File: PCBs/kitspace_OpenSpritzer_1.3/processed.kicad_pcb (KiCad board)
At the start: 2 copper layers, 57.5 x 85 mm, 30 parts

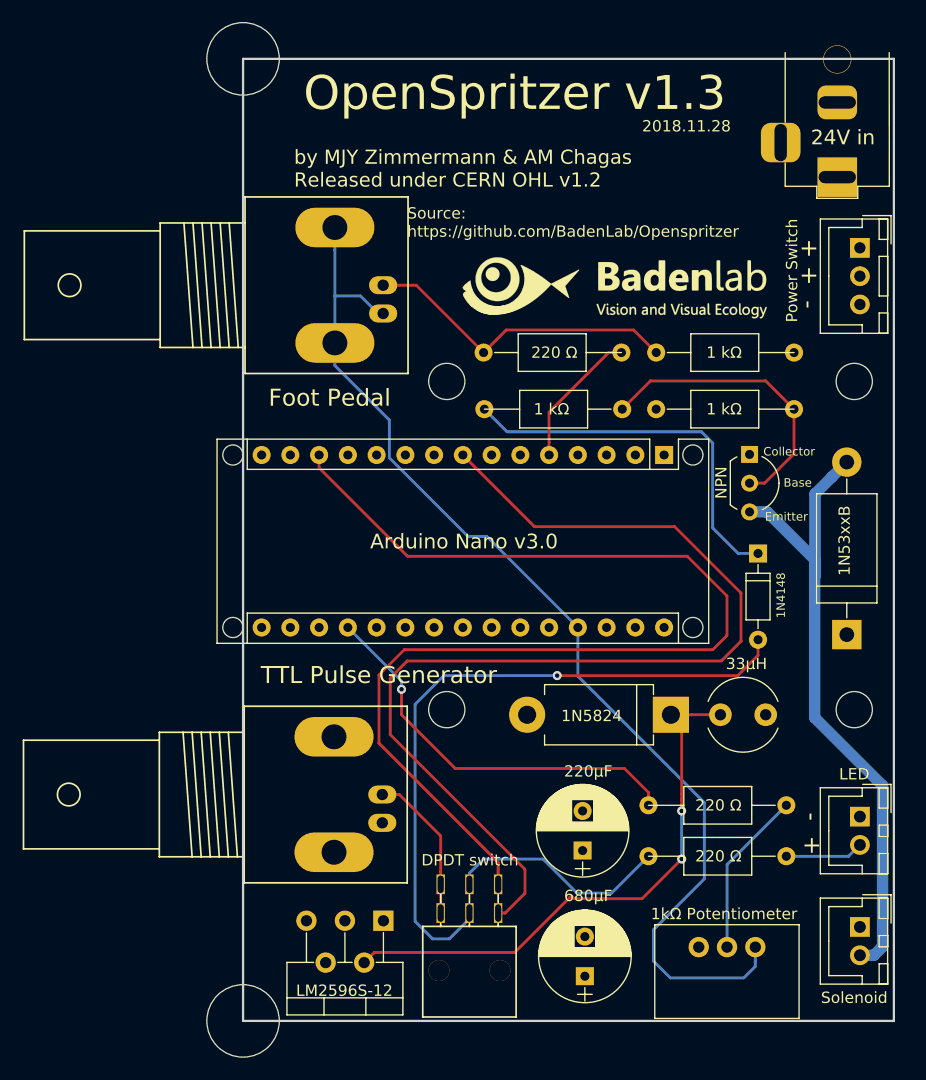
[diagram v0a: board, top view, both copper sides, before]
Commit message: recheck all circuits and clean up fill zone by rerouting the nets using freerouting and manually
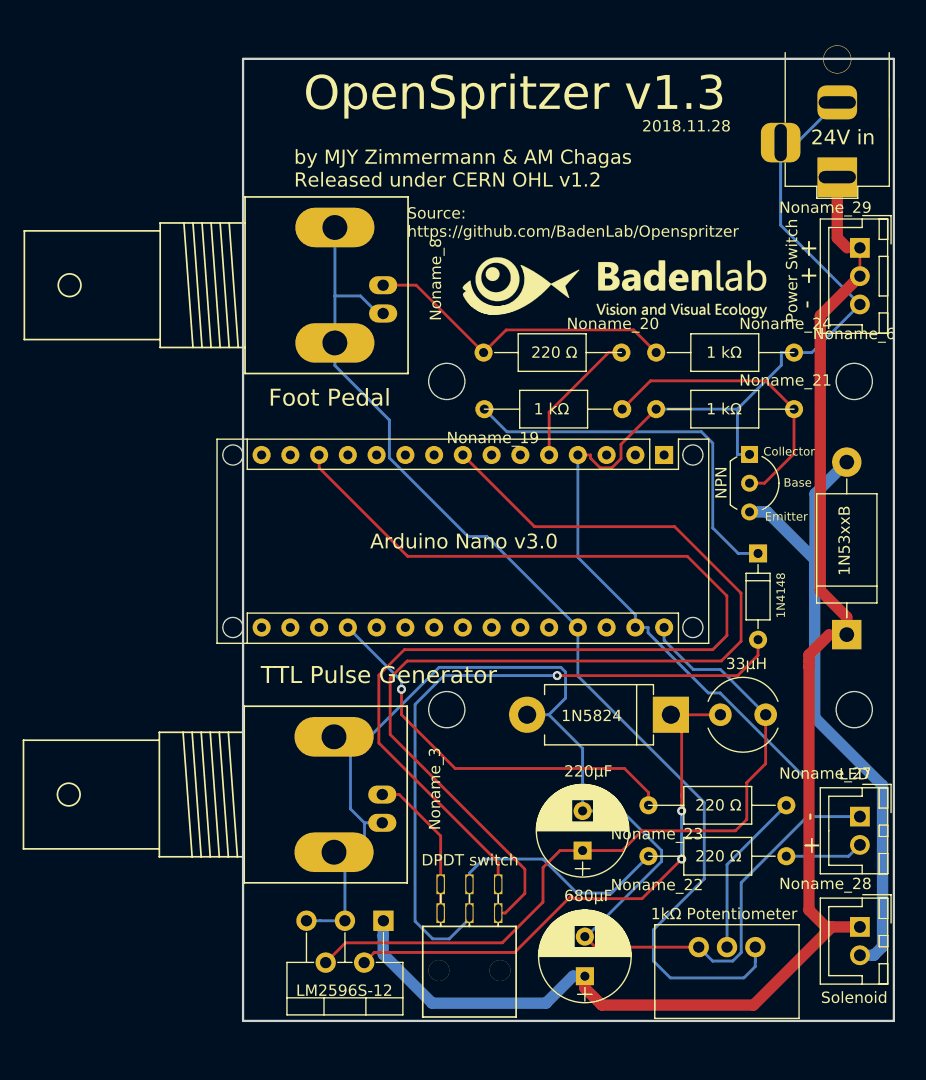
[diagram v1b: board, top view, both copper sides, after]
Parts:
- removed ?: , MountingHole:MountingHole_6.4mm_M6
- removed ?: MountingHole_6.4mm_M6, MountingHole:MountingHole_6.4mm_M6
- gave numbers to parts that had none: 27
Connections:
- NPN pad 1: (no net) -> GNDREF
- Noname_11 pad 1: (no net) -> Net-(A1-Pad30)
- Noname_11 pad 2: (no net) -> GNDREF
- Noname_12 pad 1: (no net) -> Net-(C1-Pad1)
- Noname_12 pad 2: (no net) -> GNDREF
- Noname_14 pad 2: (no net) -> GNDREF
- Noname_16 pad 1: (no net) -> Net-(C1-Pad1)
- Noname_16 pad 2: (no net) -> GNDREF
- Noname_16 pad 3: (no net) -> GNDREF
- Noname_17 pad 1: (no net) -> Net-(A1-Pad1)
- Noname_17 pad 10: (no net) -> Net-(A1-Pad10)
- Noname_17 pad 11: (no net) -> Net-(A1-Pad11)
- Noname_17 pad 12: (no net) -> Net-(A1-Pad12)
- Noname_17 pad 14: (no net) -> Net-(A1-Pad14)
- Noname_17 pad 15: (no net) -> Net-(A1-Pad15)
- Noname_17 pad 16: (no net) -> Net-(A1-Pad16)
- Noname_17 pad 17: (no net) -> Net-(A1-Pad17)
- Noname_17 pad 18: (no net) -> Net-(A1-Pad18)
- Noname_17 pad 2: (no net) -> Net-(A1-Pad2)
- Noname_17 pad 20: (no net) -> Net-(A1-Pad20)
- Noname_17 pad 21: (no net) -> Net-(A1-Pad21)
- Noname_17 pad 22: (no net) -> Net-(A1-Pad22)
- Noname_17 pad 23: (no net) -> Net-(A1-Pad23)
- Noname_17 pad 24: (no net) -> Net-(A1-Pad24)
- Noname_17 pad 25: (no net) -> Net-(A1-Pad25)
- Noname_17 pad 26: (no net) -> Net-(A1-Pad26)
- Noname_17 pad 28: (no net) -> Net-(A1-Pad28)
- Noname_17 pad 29: (no net) -> GNDREF
- Noname_17 pad 3: (no net) -> Net-(A1-Pad3)
- Noname_17 pad 30: (no net) -> Net-(A1-Pad30)
- Noname_17 pad 4: (no net) -> GNDREF
- Noname_17 pad 6: (no net) -> Net-(A1-Pad6)
- Noname_17 pad 7: (no net) -> Net-(A1-Pad7)
- Noname_17 pad 9: (no net) -> Net-(A1-Pad9)
- Noname_18 pad 1: (no net) -> Net-(A1-Pad30)
- Noname_21 pad 1: (no net) -> GNDREF
- Noname_24 pad 2: (no net) -> GNDREF
- Noname_25 pad 1: (no net) -> Net-(C1-Pad1)
- Noname_26 pad 1: (no net) -> GNDREF
- Noname_27 pad 1: (no net) -> GNDREF
- Noname_28 pad 1: (no net) -> Net-(C1-Pad1)
- Noname_29 pad 1: (no net) -> Net-(C1-Pad1)
- Noname_29 pad 2: (no net) -> Net-(C1-Pad1)
- Noname_29 pad 3: (no net) -> GNDREF
- Noname_3 pad 2: (no net) -> GNDREF
- Noname_5 pad 1: (no net) -> Net-(C1-Pad1)
- Noname_5 pad 3: (no net) -> GNDREF
- Noname_5 pad 4: (no net) -> Net-(A1-Pad30)
- Noname_5 pad 5: (no net) -> GNDREF
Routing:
- net GNDREF: track 0.00 -> 219.6 mm
- net Net-(C1-Pad1): track 0.00 -> 130.3 mm
- net Net-(A1-Pad30): track 0.00 -> 67.0 mm
- net Net-(A1-Pad27): track 97.8 -> 98.9 mm
- net Net-(D3-Pad2): track 58.3 -> 57.3 mm
